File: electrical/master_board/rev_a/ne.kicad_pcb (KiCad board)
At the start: 2 copper layers, 42.7 x 39.4 mm, 4 parts, among them CN60 HCSR04;F1x4H

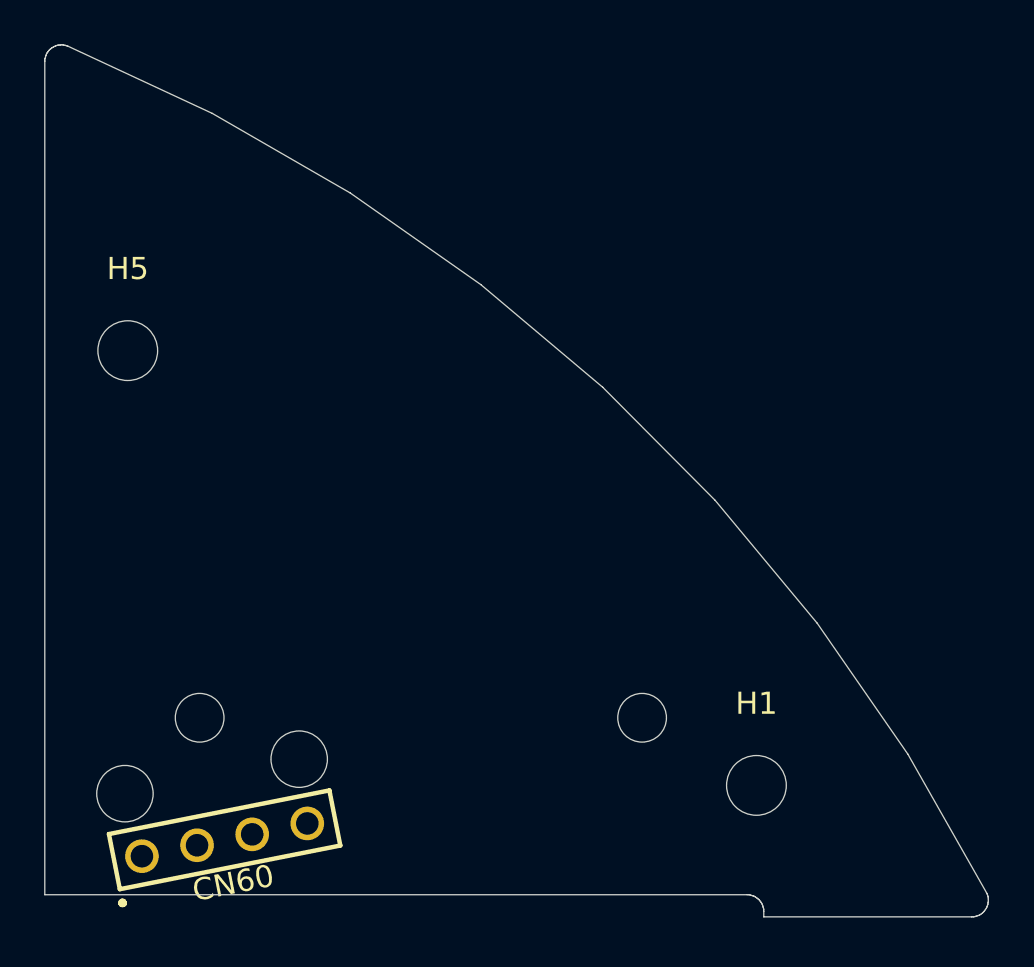
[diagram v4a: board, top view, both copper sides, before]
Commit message: Added LED's to the PCB's.
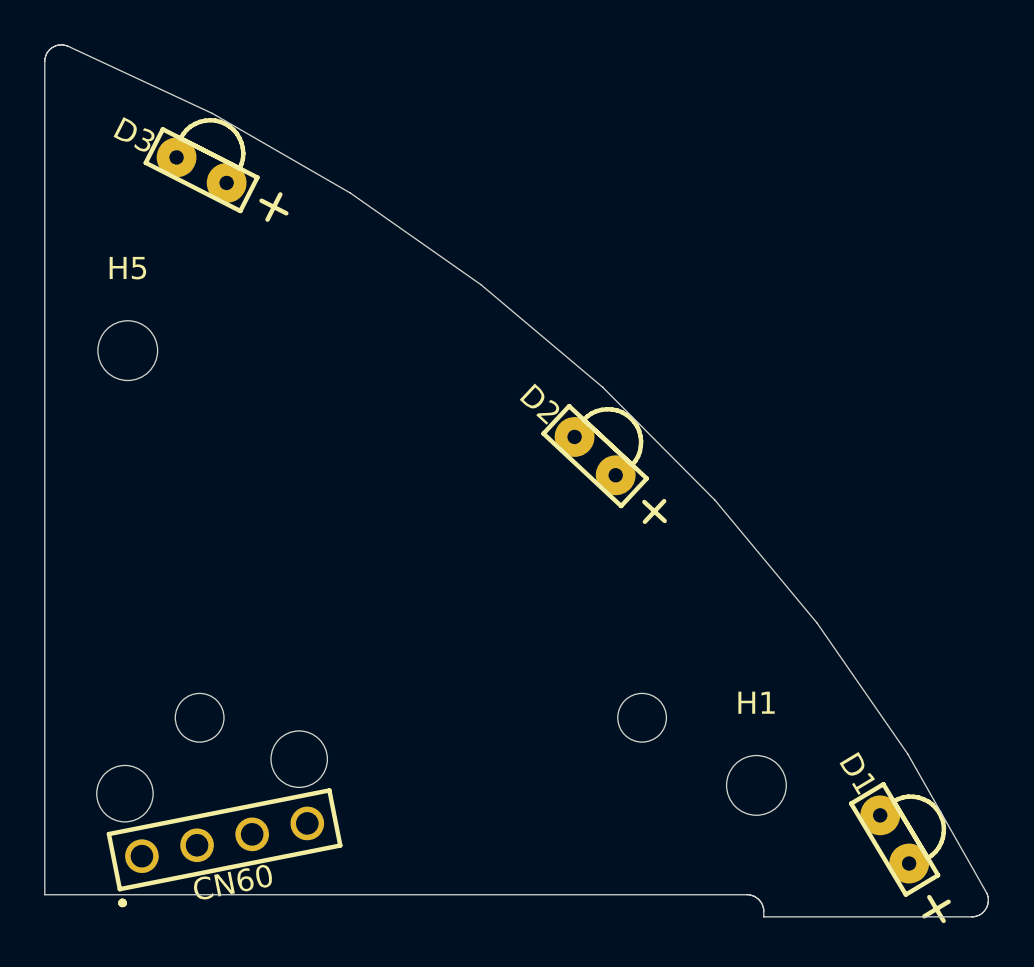
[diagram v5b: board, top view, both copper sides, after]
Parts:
- added D1: LED;GRNRA, HR2:LED_GRNRA, F.Cu at (168.4, 60.5)
- added D2: LED;GRNRA, HR2:LED_GRNRA, F.Cu at (154.9, 43.2)
- added D3: LED;GRNRA, HR2:LED_GRNRA, F.Cu at (137.1, 30.2)
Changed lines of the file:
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@@
     (tracks 0)
     (zones 0)
-    (modules 4)
+    (modules 7)
     (nets 5)
   )
@@
     (add_net "Net-(CN60-Pad4)")
   )
+  (module HR2:LED_GRNRA (layer F.Cu)
+    (at 137.0883 30.2471 63)
+    (fp_text reference D3 (at 0 -3.4 153) (layer F.SilkS)
+      (effects (font (size 1 1) (thickness 0.2)))
+    )
+    (fp_text value LED;GRNRA (at 0 0 63) (layer F.Fab)
+      (effects (font (size 1 1) (thickness 0.2)))
+    )
+    (fp_line (start -0.85 -2.4) (end 0.85 -2.4) (layer F.SilkS) (width 0.2))
+    (fp_line (start -0.85 2.4) (end -0.85 -2.4) (layer F.SilkS) (width 0.2))
+    (fp_line (start 0.85 2.4) (end -0.85 2.4) (layer F.SilkS) (width 0.2))
+    (fp_line (start 0.85 -2.4) (end 0.85 2.4) (layer F.SilkS) (width 0.2))
+    (fp_line (start 0.85 -1.5) (end 0.85 1.5) (layer F.SilkS) (width 0.2))
+    (fp_line (start 1.08 -1.48) (end 0.85 -1.5) (layer F.SilkS) (width 0.2))
+    (fp_line (start 1.31 -1.43) (end 1.08 -1.48) (layer F.SilkS) (width 0.2))
+    (fp_line (start 1.53 -1.34) (end 1.31 -1.43) (layer F.SilkS) (width 0.2))
+    (fp_line (start 1.73 -1.21) (end 1.53 -1.34) (layer F.SilkS) (width 0.2))
+    (fp_line (start 1.91 -1.06) (end 1.73 -1.21) (layer F.SilkS) (width 0.2))
+    (fp_line (start 2.06 -0.88) (end 1.91 -1.06) (layer F.SilkS) (width 0.2))
+    (fp_line (start 2.19 -0.68) (end 2.06 -0.88) (layer F.SilkS) (width 0.2))
+    (fp_line (start 2.28 -0.46) (end 2.19 -0.68) (layer F.SilkS) (width 0.2))
+    (fp_line (start 2.33 -0.23) (end 2.28 -0.46) (layer F.SilkS) (width 0.2))
+    (fp_line (start 2.35 0) (end 2.33 -0.23) (layer F.SilkS) (width 0.2))
+    (fp_line (start 2.33 0.23) (end 2.35 0) (layer F.SilkS) (width 0.2))
+    (fp_line (start 2.28 0.46) (end 2.33 0.23) (layer F.SilkS) (width 0.2))
+    (fp_line (start 2.19 0.68) (end 2.28 0.46) (layer F.SilkS) (width 0.2))
+    (fp_line (start 2.06 0.88) (end 2.19 0.68) (layer F.SilkS) (width 0.2))
+    (fp_line (start 1.91 1.06) (end 2.06 0.88) (layer F.SilkS) (width 0.2))
+    (fp_line (start 1.73 1.21) (end 1.91 1.06) (layer F.SilkS) (width 0.2))
+    (fp_line (start 1.53 1.34) (end 1.73 1.21) (layer F.SilkS) (width 0.2))
+    (fp_line (start 1.31 1.43) (end 1.53 1.34) (layer F.SilkS) (width 0.2))
+    (fp_line (start 1.08 1.48) (end 1.31 1.43) (layer F.SilkS) (width 0.2))
+    (fp_line (start 0.85 1.5) (end 1.08 1.48) (layer F.SilkS) (width 0.2))
+    (fp_line (start -0.64 3.67) (end 0.64 3.67) (layer F.SilkS) (width 0.2))
+    (fp_line (start 0 4.3) (end 0 3.04) (layer F.SilkS) (width 0.2))
+    (pad - thru_hole circle (at 0 -1.27 63) (size 1.8 1.8) (drill 0.65) (layers *.Cu *.Mask))
+    (pad + thru_hole circle (at 0 1.27 63) (size 1.8 1.8) (drill 0.65) (layers *.Cu *.Mask))
+  )
+  (module HR2:LED_GRNRA (layer F.Cu)
+    (at 154.878 43.1722 47)
+    (fp_text reference D2 (at 0 -3.4 137) (layer F.SilkS)
+      (effects (font (size 1 1) (thickness 0.2)))
+    )
+    (fp_text value LED;GRNRA (at 0 0 47) (layer F.Fab)
+      (effects (font (size 1 1) (thickness 0.2)))
+    )
+    (fp_line (start -0.85 -2.4) (end 0.85 -2.4) (layer F.SilkS) (width 0.2))
+    (fp_line (start -0.85 2.4) (end -0.85 -2.4) (layer F.SilkS) (width 0.2))
+    (fp_line (start 0.85 2.4) (end -0.85 2.4) (layer F.SilkS) (width 0.2))
+    (fp_line (start 0.85 -2.4) (end 0.85 2.4) (layer F.SilkS) (width 0.2))
+    (fp_line (start 0.85 -1.5) (end 0.85 1.5) (layer F.SilkS) (width 0.2))
+    (fp_line (start 1.08 -1.48) (end 0.85 -1.5) (layer F.SilkS) (width 0.2))
+    (fp_line (start 1.31 -1.43) (end 1.08 -1.48) (layer F.SilkS) (width 0.2))
+    (fp_line (start 1.53 -1.34) (end 1.31 -1.43) (layer F.SilkS) (width 0.2))
+    (fp_line (start 1.73 -1.21) (end 1.53 -1.34) (layer F.SilkS) (width 0.2))
+    (fp_line (start 1.91 -1.06) (end 1.73 -1.21) (layer F.SilkS) (width 0.2))
+    (fp_line (start 2.06 -0.88) (end 1.91 -1.06) (layer F.SilkS) (width 0.2))
+    (fp_line (start 2.19 -0.68) (end 2.06 -0.88) (layer F.SilkS) (width 0.2))
+    (fp_line (start 2.28 -0.46) (end 2.19 -0.68) (layer F.SilkS) (width 0.2))
+    (fp_line (start 2.33 -0.23) (end 2.28 -0.46) (layer F.SilkS) (width 0.2))
+    (fp_line (start 2.35 0) (end 2.33 -0.23) (layer F.SilkS) (width 0.2))
+    (fp_line (start 2.33 0.23) (end 2.35 0) (layer F.SilkS) (width 0.2))
+    (fp_line (start 2.28 0.46) (end 2.33 0.23) (layer F.SilkS) (width 0.2))
+    (fp_line (start 2.19 0.68) (end 2.28 0.46) (layer F.SilkS) (width 0.2))
+    (fp_line (start 2.06 0.88) (end 2.19 0.68) (layer F.SilkS) (width 0.2))
+    (fp_line (start 1.91 1.06) (end 2.06 0.88) (layer F.SilkS) (width 0.2))
+    (fp_line (start 1.73 1.21) (end 1.91 1.06) (layer F.SilkS) (width 0.2))
+    (fp_line (start 1.53 1.34) (end 1.73 1.21) (layer F.SilkS) (width 0.2))
+    (fp_line (start 1.31 1.43) (end 1.53 1.34) (layer F.SilkS) (width 0.2))
+    (fp_line (start 1.08 1.48) (end 1.31 1.43) (layer F.SilkS) (width 0.2))
+    (fp_line (start 0.85 1.5) (end 1.08 1.48) (layer F.SilkS) (width 0.2))
+    (fp_line (start -0.64 3.67) (end 0.64 3.67) (layer F.SilkS) (width 0.2))
+    (fp_line (start 0 4.3) (end 0 3.04) (layer F.SilkS) (width 0.2))
+    (pad - thru_hole circle (at 0 -1.27 47) (size 1.8 1.8) (drill 0.65) (layers *.Cu *.Mask))
+    (pad + thru_hole circle (at 0 1.27 47) (size 1.8 1.8) (drill 0.65) (layers *.Cu *.Mask))
+  )
+  (module HR2:LED_GRNRA (layer F.Cu)
+    (at 168.416 60.5 31)
+    (fp_text reference D1 (at 0.1 -3.4 121) (layer F.SilkS)
+      (effects (font (size 1 1) (thickness 0.2)))
+    )
+    (fp_text value LED;GRNRA (at 0 0 31) (layer F.Fab)
+      (effects (font (size 1 1) (thickness 0.2)))
+    )
+    (fp_line (start -0.85 -2.4) (end 0.85 -2.4) (layer F.SilkS) (width 0.2))
+    (fp_line (start -0.85 2.4) (end -0.85 -2.4) (layer F.SilkS) (width 0.2))
+    (fp_line (start 0.85 2.4) (end -0.85 2.4) (layer F.SilkS) (width 0.2))
+    (fp_line (start 0.85 -2.4) (end 0.85 2.4) (layer F.SilkS) (width 0.2))
+    (fp_line (start 0.85 -1.5) (end 0.85 1.5) (layer F.SilkS) (width 0.2))
+    (fp_line (start 1.08 -1.48) (end 0.85 -1.5) (layer F.SilkS) (width 0.2))
+    (fp_line (start 1.31 -1.43) (end 1.08 -1.48) (layer F.SilkS) (width 0.2))
+    (fp_line (start 1.53 -1.34) (end 1.31 -1.43) (layer F.SilkS) (width 0.2))
+    (fp_line (start 1.73 -1.21) (end 1.53 -1.34) (layer F.SilkS) (width 0.2))
+    (fp_line (start 1.91 -1.06) (end 1.73 -1.21) (layer F.SilkS) (width 0.2))
+    (fp_line (start 2.06 -0.88) (end 1.91 -1.06) (layer F.SilkS) (width 0.2))
+    (fp_line (start 2.19 -0.68) (end 2.06 -0.88) (layer F.SilkS) (width 0.2))
+    (fp_line (start 2.28 -0.46) (end 2.19 -0.68) (layer F.SilkS) (width 0.2))
+    (fp_line (start 2.33 -0.23) (end 2.28 -0.46) (layer F.SilkS) (width 0.2))
+    (fp_line (start 2.35 0) (end 2.33 -0.23) (layer F.SilkS) (width 0.2))
+    (fp_line (start 2.33 0.23) (end 2.35 0) (layer F.SilkS) (width 0.2))
+    (fp_line (start 2.28 0.46) (end 2.33 0.23) (layer F.SilkS) (width 0.2))
+    (fp_line (start 2.19 0.68) (end 2.28 0.46) (layer F.SilkS) (width 0.2))
+    (fp_line (start 2.06 0.88) (end 2.19 0.68) (layer F.SilkS) (width 0.2))
+    (fp_line (start 1.91 1.06) (end 2.06 0.88) (layer F.SilkS) (width 0.2))
+    (fp_line (start 1.73 1.21) (end 1.91 1.06) (layer F.SilkS) (width 0.2))
+    (fp_line (start 1.53 1.34) (end 1.73 1.21) (layer F.SilkS) (width 0.2))
+    (fp_line (start 1.31 1.43) (end 1.53 1.34) (layer F.SilkS) (width 0.2))
+    (fp_line (start 1.08 1.48) (end 1.31 1.43) (layer F.SilkS) (width 0.2))
+    (fp_line (start 0.85 1.5) (end 1.08 1.48) (layer F.SilkS) (width 0.2))
+    (fp_line (start -0.64 3.67) (end 0.64 3.67) (layer F.SilkS) (width 0.2))
+    (fp_line (start 0 4.3) (end 0 3.04) (layer F.SilkS) (width 0.2))
+    (pad - thru_hole circle (at 0 -1.27 31) (size 1.8 1.8) (drill 0.65) (layers *.Cu *.Mask))
+    (pad + thru_hole circle (at 0 1.27 31) (size 1.8 1.8) (drill 0.65) (layers *.Cu *.Mask))
+  )
   (module HR2:GROVE20x20 (layer B.Cu)

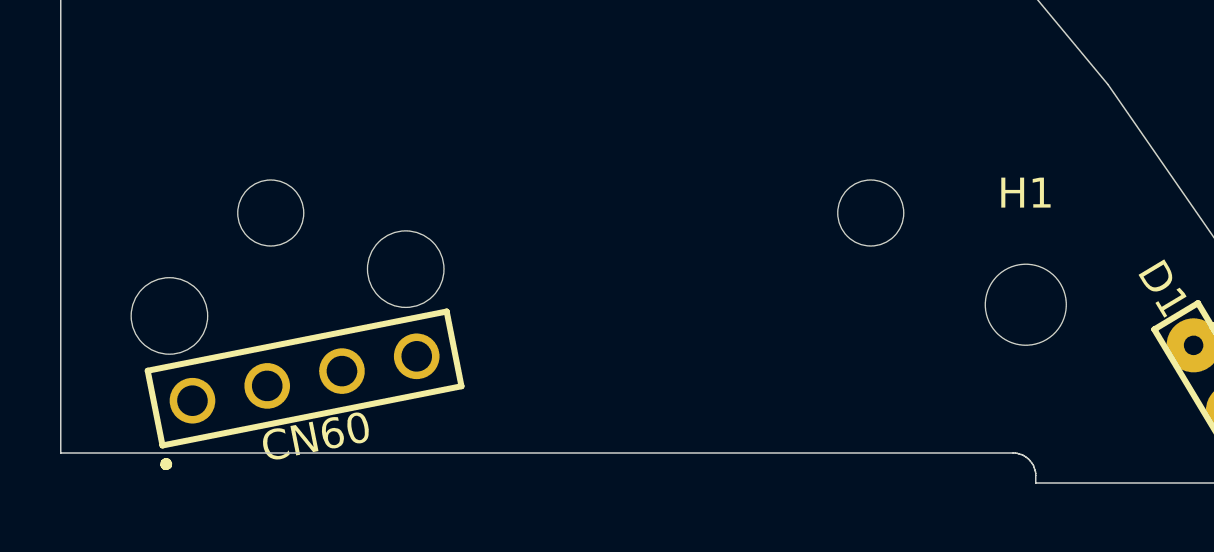
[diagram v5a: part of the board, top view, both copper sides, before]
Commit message: Got Bridge connectors installed on PCB's. Tweaking still required.
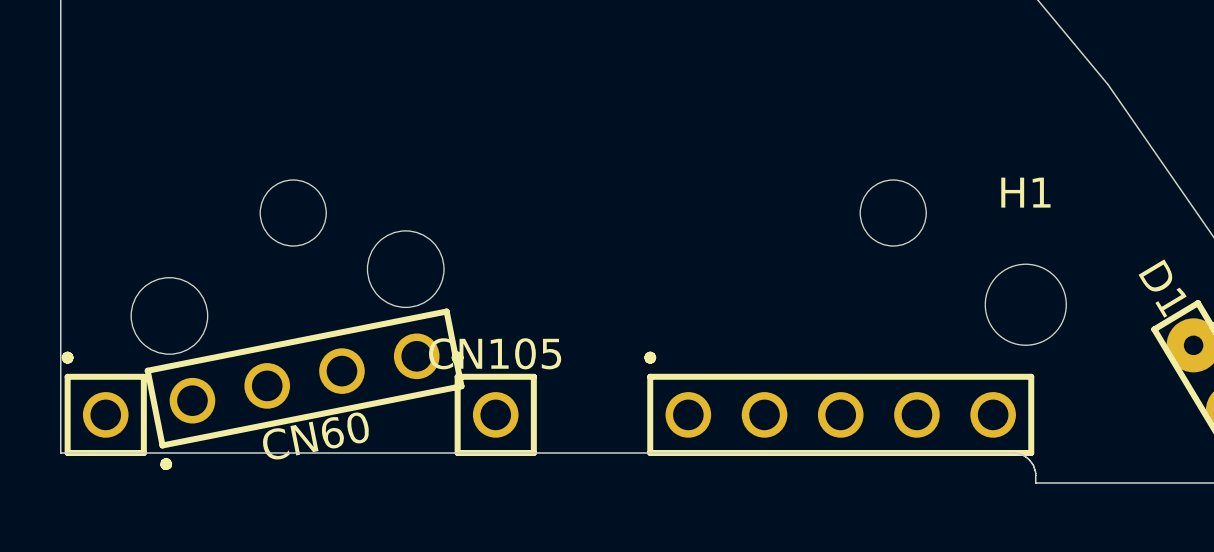
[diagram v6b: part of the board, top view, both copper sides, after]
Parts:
- added CN105: BRIDGE_NE_OUTER;2xM1x1+M1x5, HR2:BRIDGE_NE_OUTER_2xM1x1+M1x5, F.Cu at (144.5, 61.7)
- moved GV2 0.75 mm to (147.8, 55.0)
